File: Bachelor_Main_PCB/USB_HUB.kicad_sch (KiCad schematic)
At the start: 15 parts, among them J11 M20-9990245, U6 USB2514B-I/M2

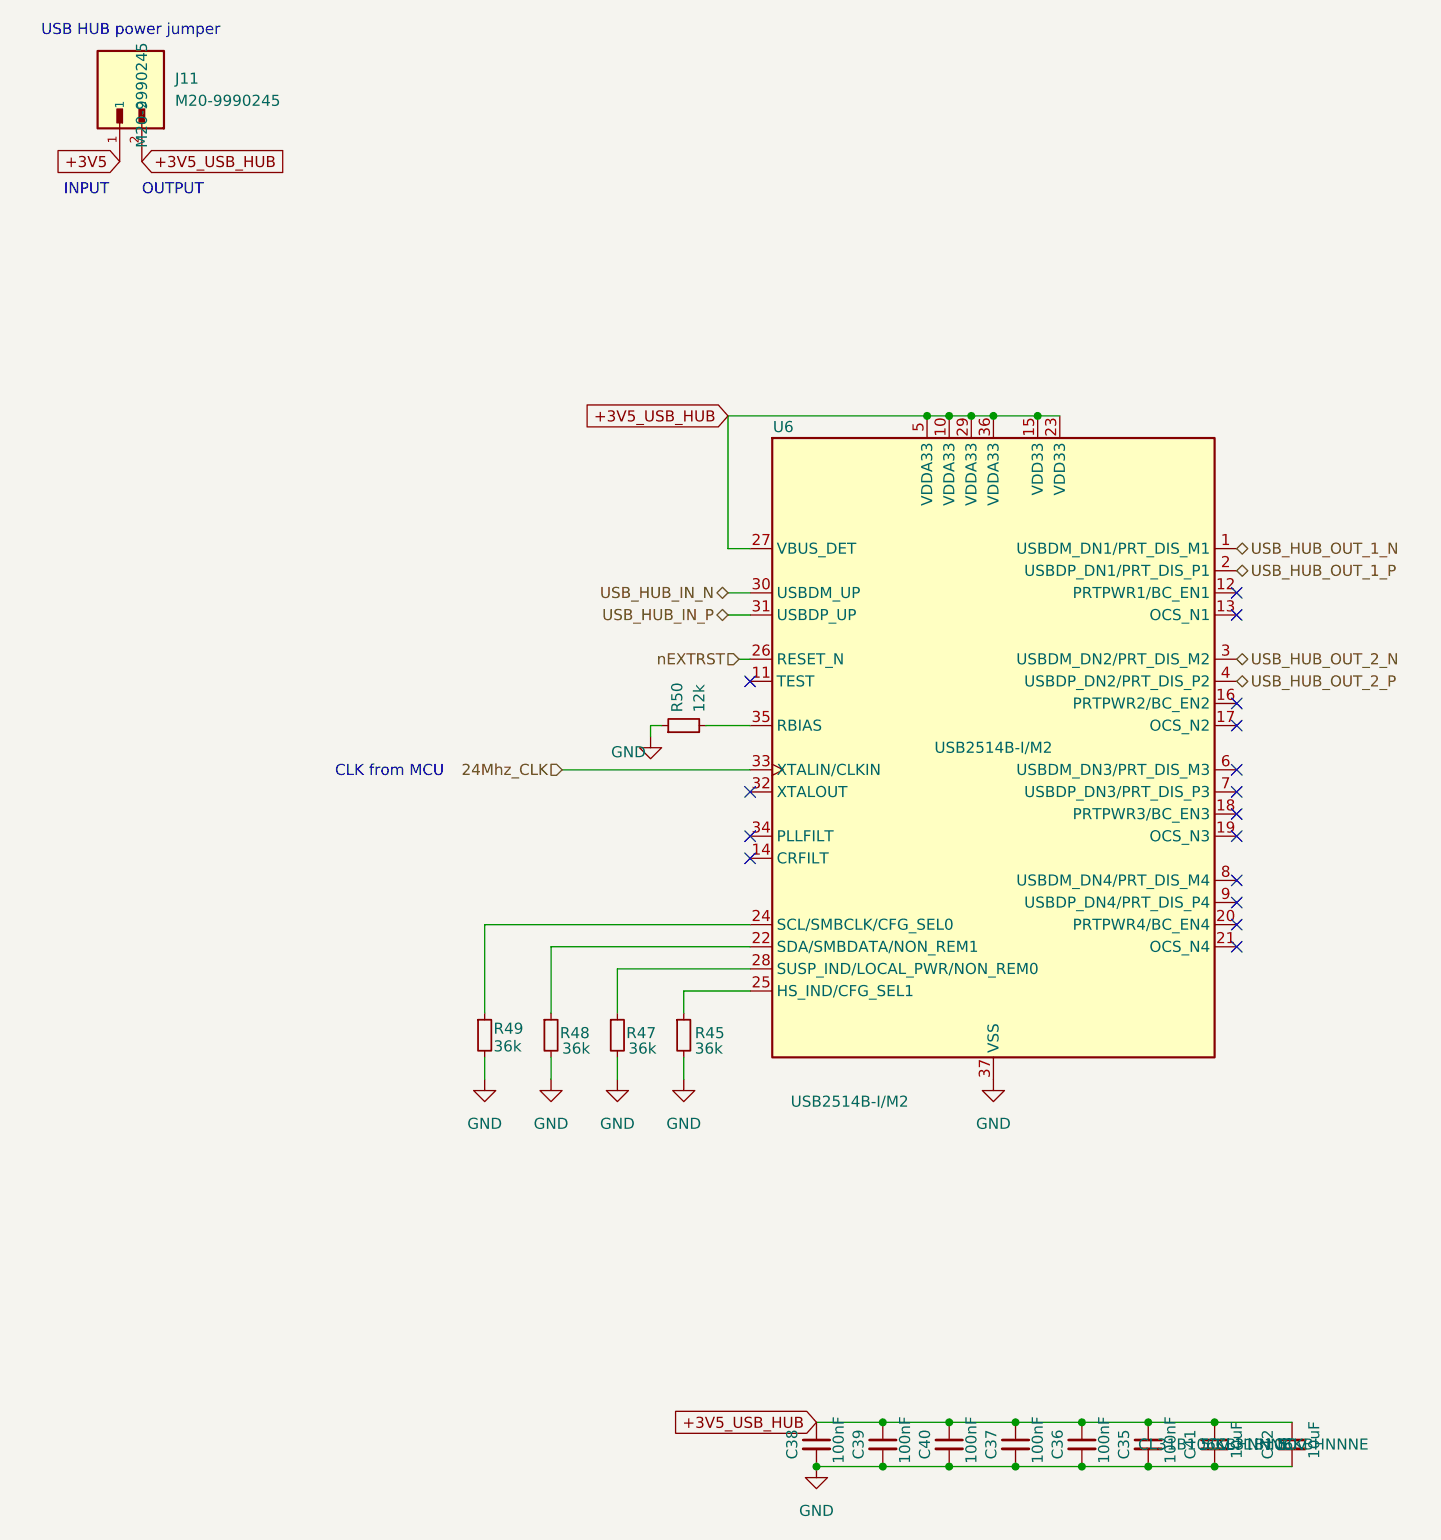
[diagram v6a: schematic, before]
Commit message: Add 1% tolerance field to high tolerance resistors
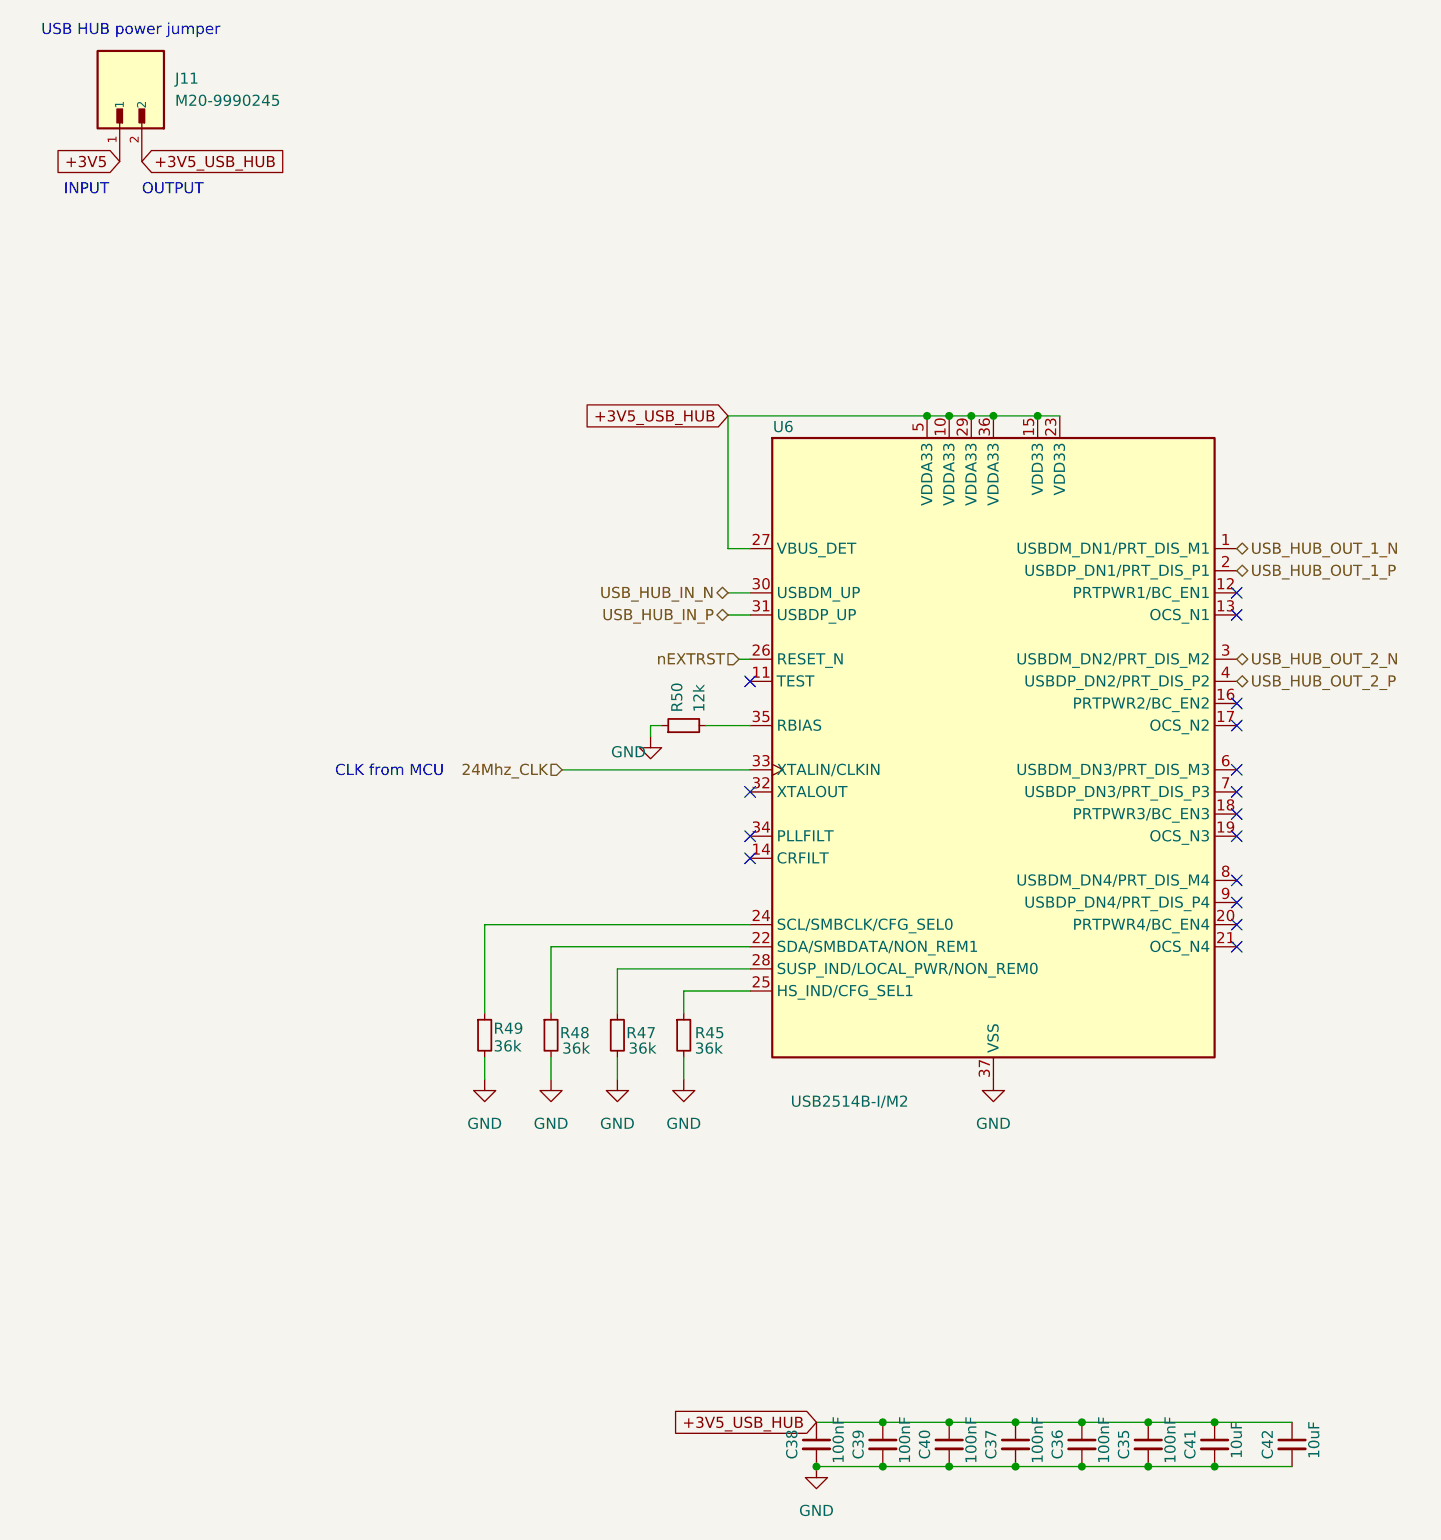
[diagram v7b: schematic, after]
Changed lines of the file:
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@@
 					(size 1.27 1.27)
 				)
+				(hide yes)
 			)
 		)
@@
 					(size 1.27 1.27)
 				)
+				(hide yes)
 			)
 		)
@@
 					(size 1.27 1.27)
 				)
+				(hide yes)
 			)
 		)
@@
 					(size 1.27 1.27)
 				)
+				(hide yes)
 			)
 		)
@@
 					(size 1.27 1.27)
 				)
+				(hide yes)
 			)
 		)
@@
 					(size 1.27 1.27)
 				)
-			)
-		)
+				(hide yes)
+			)
+		)

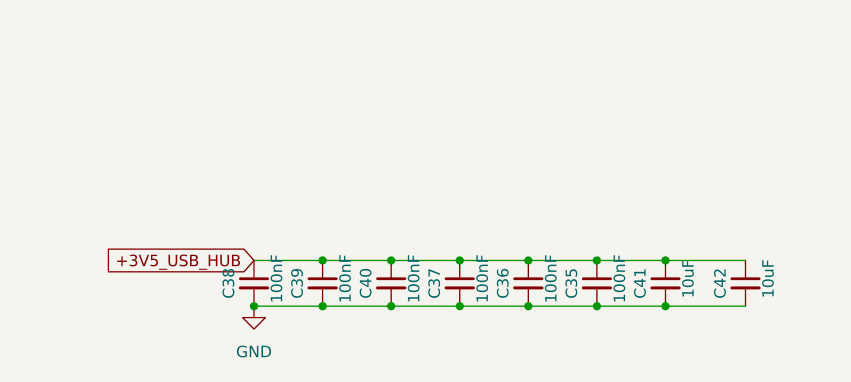
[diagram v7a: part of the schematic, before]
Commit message: Add Part-no to all caps and replaced 15pF on bugg with 33pF
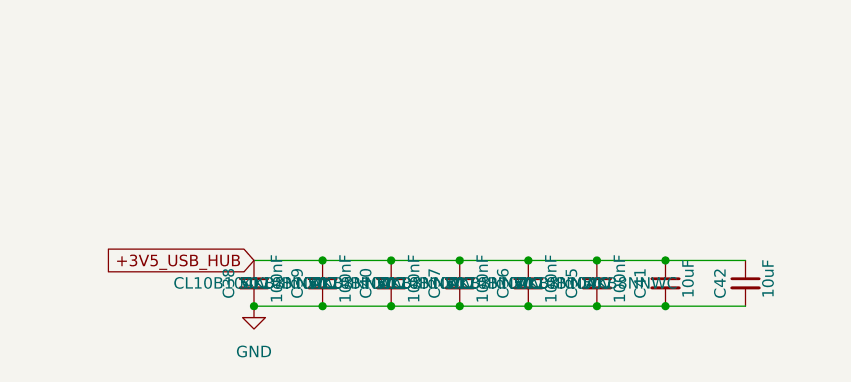
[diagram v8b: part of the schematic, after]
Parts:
- C35, C36, C37, C38, C39, C40: Part-no (none) -> CL10B104KB8NNWC; Voltage rating (none) -> 50v
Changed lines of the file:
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@@
+			)
+		)
+		(property "Part-no" "CL10B104KB8NNWC"
+			(at 125.73 180.34 0)
+			(effects
+				(font
+					(size 1.27 1.27)
+				)
+			)
+		)
+		(property "Voltage rating" "50v"
+			(at 125.73 180.34 0)
+			(effects
+				(font
+					(size 1.27 1.27)
+				)
 			)
 		)
@@
 			)
 		)
+		(property "Part-no" "CL10B104KB8NNWC"
+			(at 133.35 180.34 0)
+			(effects
+				(font
+					(size 1.27 1.27)
+				)
+			)
+		)
+		(property "Voltage rating" "50v"
+			(at 133.35 180.34 0)
+			(effects
+				(font
+					(size 1.27 1.27)
+				)
+			)
+		)
 		(pin "2"
 		)
@@
 			)
 		)
+		(property "Part-no" "CL10B104KB8NNWC"
+			(at 148.59 180.34 0)
+			(effects
+				(font
+					(size 1.27 1.27)
+				)
+			)
+		)
+		(property "Voltage rating" "50v"
+			(at 148.59 180.34 0)
+			(effects
+				(font
+					(size 1.27 1.27)
+				)
+			)
+		)
 		(pin "2"
 		)
@@
 			)
 		)
+		(property "Part-no" "CL10B104KB8NNWC"
+			(at 110.49 180.34 0)
+			(effects
+				(font
+					(size 1.27 1.27)
+				)
+			)
+		)
+		(property "Voltage rating" "50v"
+			(at 110.49 180.34 0)
+			(effects
+				(font
+					(size 1.27 1.27)
+				)
+			)
+		)
 		(pin "2"
 		)
@@
 			)
 		)
+		(property "Part-no" "CL10B104KB8NNWC"
+			(at 118.11 180.34 0)
+			(effects
+				(font
+					(size 1.27 1.27)
+				)
+			)
+		)
+		(property "Voltage rating" "50v"
+			(at 118.11 180.34 0)
+			(effects
+				(font
+					(size 1.27 1.27)
+				)
+			)
+		)
 		(pin "2"
 		)
@@
 			)
 		)
+		(property "Part-no" "CL10B104KB8NNWC"
+			(at 140.97 180.34 0)
+			(effects
+				(font
+					(size 1.27 1.27)
+				)
+			)
+		)
+		(property "Voltage rating" "50v"
+			(at 140.97 180.34 0)
+			(effects
+				(font
+					(size 1.27 1.27)
+				)
+			)
+		)
